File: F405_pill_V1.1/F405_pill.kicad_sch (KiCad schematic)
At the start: 50 parts, among them J1 Conn_01x04_Male, J2 Conn_01x04_Male, J4 TYPE-C-31-M-12, U1 STM32F405RGTx, U2 MAX3051EKA+T, U3 LM1117-3.3, U4 STM32F405_pill, U5 HT7550-1, Y1 Crystal_GND24

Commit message: minor edits
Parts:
- removed C23: C_Polarized_Small, Capacitor_SMD:C_0603_1608Metric, symbol Device:C_Polarized_Small
- C22: value C_Polarized_Small -> 10u
- U2: value MAX3051EKA+T -> TJA1050T/CM,118; LCSC C112005 -> C6952
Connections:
- net DUAL1: now also U1.29 (PB10); no longer U1.24 (PC4)
- net DUAL2: now also U1.30 (PB11); no longer U1.25 (PC5)
- net PB10 renamed PC4
- net PC4: now also U1.24 (PC4); no longer U1.29 (PB10)
- net PB11 renamed PC5
- net PC5: now also U1.25 (PC5); no longer U1.30 (PB11)
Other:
- note added: "60 ohm split termination"
- note added: "NC GND V3V3 ADC SPI1SCK DAC TIM2 ADC SPI1MISO TIM3 JP3 / FET TEMP A_PHC_VSENSE JP2 / MOTOR TEMP / SPI1MOSI A_PHB_VSENSE A_PHA_VSENSE A_SHC_AMP A_SHB_AMP A_SHA_AMP VSENSE A_THROTTLE JP3 / FET TEMP HALL_C HALL_B HALL_A NC"
- note removed: "CONFIRM: Does david want to use MAX3051 ?"
- note removed: "CONFIRM: ridiculously large LDO?"
- note removed: "NC GND V3V3 ADC SPI1 DAC TIM2 ADC SPI1MISO TIM3 JP3 / FET TEMP A_PHC_VSENSE JP2 / MOTOR TEMP A_PHB_VSENSE A_PHA_VSENSE A_SHC_AMP A_SHB_AMP A_SHA_AMP VSENSE A_THROTTLE JP3 / FET TEMP HALL_C HALL_B HALL_A NC"
- note removed: "NOTE: Split termination may be unnecessary"

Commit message: minor part changes
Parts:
- removed C16: 10u, Capacitor_Tantalum_SMD:CP_EIA-3216-18_Kemet-A, symbol Device:C_Polarized_Small
- removed U5: HT7550-1, Package_TO_SOT_SMD:SOT-89-3, symbol Regulator_Linear:L78L10_SOT89
- added C22: 10u, Capacitor_SMD:C_0603_1608Metric, symbol Device:C_Polarized_Small
- added U5: HT7550, Package_TO_SOT_SMD:SOT-89-3, symbol Regulator_Linear:L79L08_SOT89
- R1, R2: LCSC C25086 -> C25744
- R3, R4: value 60 ohm -> 100Ω; footprint Resistor_SMD:R_0603_1608Metric -> Resistor_SMD:R_0402_1005Metric; LCSC C4216 -> C25076
- U2: footprint Package_TO_SOT_SMD:SOT-23-8 -> Package_SO:SOIC-8_3.9x4.9mm_P1.27mm
- renumbered C22 to C16
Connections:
- net +3V3: now also C22.1
- net +5V: now also U5.2 (VI)
- net GND: now also C22.2, U5.1 (GND)
- net VDO_I: now also U5.3 (VO)
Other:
- note added: "100 ohm split termination"
- note added: "Changes: Xtal caps from 18pF to 12pF Separate the two LEDs from the single resistor CAN spike protection RC between GND and pb12 to stop false trips PC12->PA15 to drive LED Increased functionality of several header pins"
- note added: "DECOUPLING"
- note added: "OVERVOLTAGE FILTER"
- note removed: "60 ohm split termination"
- note removed: "CONFIRM: correct wiring?"
- note removed: "Changes: Xtal caps from 18pF to 12pF Separate the two LEDs from the single resistor New CAN, with spike protection RC between GND and pb12 to stop false trips PC12->PA15 to drive LED Increased functionality of several header pins"
- note removed: "No Parasites Overvoltage filter"
- moved on the sheet: C21, J2, R6

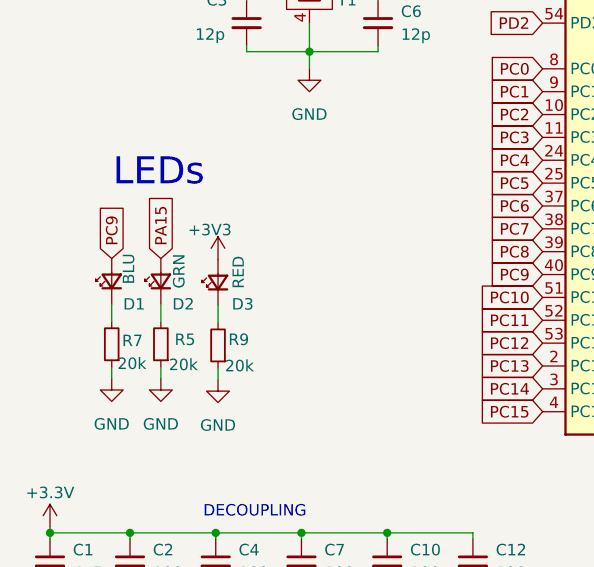
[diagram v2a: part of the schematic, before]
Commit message: changed LEDs
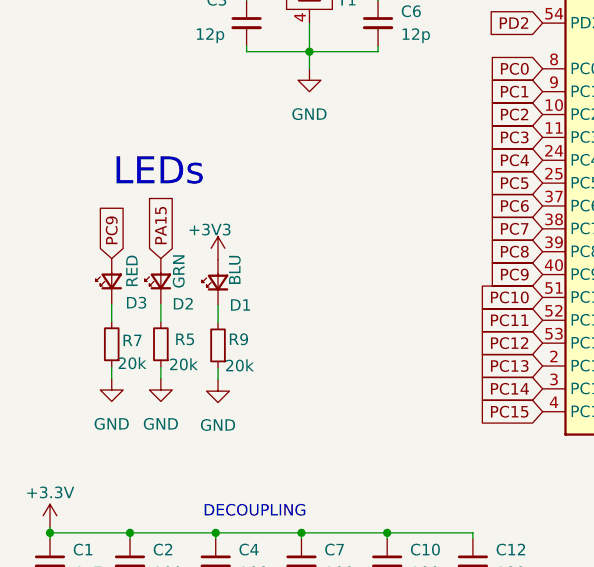
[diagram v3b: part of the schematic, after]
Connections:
- net +3V3: now also D1.2 (A); no longer D3.2 (A)
- net PC9: now also D3.2 (A); no longer D1.2 (A)
- net at R7.2: now also D3.1 (K); no longer D1.1 (K)
- net at R9.2: now also D1.1 (K); no longer D3.1 (K)
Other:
- moved on the sheet: D1, D3
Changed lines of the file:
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@@
     (pin "1")
   )
-  (symbol (lib_id "Device:LED_Small") (at 25.146 95.631 90) (unit 1)
+  (symbol (lib_id "Device:LED_Small") (at 36.957 95.758 90) (unit 1)
     (in_bom yes) (on_board yes)
-    (property "Reference" "D1" (id 0) (at 26.416 98.171 90)
+    (property "Reference" "D1" (id 0) (at 38.227 98.298 90)
       (effects (font (size 1.27 1.27)) (justify right))
     )
-    (property "Value" "BLU" (id 1) (at 27.051 94.234 0))
-    (property "Footprint" "LED_SMD:LED_0603_1608Metric" (id 2) (at 25.146 95.631 90)
+    (property "Value" "BLU" (id 1) (at 38.862 94.361 0))
+    (property "Footprint" "LED_SMD:LED_0603_1608Metric" (id 2) (at 36.957 95.758 90)
       (effects (font (size 1.27 1.27)) hide)
     )
-    (property "Datasheet" "https://datasheet.lcsc.com/lcsc/2008201033_Foshan-NationStar-Optoelectronics-NCD0402B1_C130724.pdf" (id 3) (at 25.146 95.631 90)
+    (property "Datasheet" "https://datasheet.lcsc.com/lcsc/2008201033_Foshan-NationStar-Optoelectronics-NCD0402B1_C130724.pdf" (id 3) (at 36.957 95.758 90)
       (effects (font (size 1.27 1.27)) hide)
     )
-    (property "LCSC" "C72041" (id 6) (at 25.146 95.631 0)
+    (property "LCSC" "C72041" (id 6) (at 36.957 95.758 0)
       (effects (font (size 1.27 1.27)) hide)
     )
@@
     (pin "2")
   )
-  (symbol (lib_id "Device:LED_Small") (at 36.957 95.758 90) (unit 1)
+  (symbol (lib_id "Device:LED_Small") (at 25.146 95.631 90) (unit 1)
     (in_bom yes) (on_board yes)
-    (property "Reference" "D3" (id 0) (at 38.481 98.171 90)
+    (property "Reference" "D3" (id 0) (at 26.67 98.044 90)
       (effects (font (size 1.27 1.27)) (justify right))
     )
-    (property "Value" "RED" (id 1) (at 39.243 94.615 0))
-    (property "Footprint" "LED_SMD:LED_0603_1608Metric" (id 2) (at 36.957 95.758 90)
+    (property "Value" "RED" (id 1) (at 27.432 94.488 0))
+    (property "Footprint" "LED_SMD:LED_0603_1608Metric" (id 2) (at 25.146 95.631 90)
       (effects (font (size 1.27 1.27)) hide)
     )
-    (property "Datasheet" "https://datasheet.lcsc.com/lcsc/2008201033_Foshan-NationStar-Optoelectronics-NCD0603G2_C87326.pdf" (id 3) (at 36.957 95.758 90)
+    (property "Datasheet" "https://datasheet.lcsc.com/lcsc/2008201033_Foshan-NationStar-Optoelectronics-NCD0603G2_C87326.pdf" (id 3) (at 25.146 95.631 90)
       (effects (font (size 1.27 1.27)) hide)
     )
-    (property "LCSC" "C2286" (id 6) (at 36.957 95.758 0)
+    (property "LCSC" "C2286" (id 6) (at 25.146 95.631 0)
       (effects (font (size 1.27 1.27)) hide)
     )

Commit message: removed directory
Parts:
- JP1, JP2: now left out of the parts list
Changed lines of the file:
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@@
   )
   (symbol (lib_id "Jumper:Jumper_2_Open") (at 53.975 28.829 0) (mirror y) (unit 1)
-    (in_bom yes) (on_board yes)
+    (in_bom no) (on_board yes)
     (property "Reference" "JP2" (id 0) (at 55.245 26.289 0)
       (effects (font (size 1.27 1.27)) (justify left))
@@
   )
   (symbol (lib_id "Jumper:Jumper_2_Open") (at 40.005 28.829 90) (mirror x) (unit 1)
-    (in_bom yes) (on_board yes)
+    (in_bom no) (on_board yes)
     (property "Reference" "JP1" (id 0) (at 38.735 25.019 90)
       (effects (font (size 1.27 1.27)) (justify left))
